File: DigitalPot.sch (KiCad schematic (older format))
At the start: 4 parts, among them IC24 AD5160BRJZ5-R2

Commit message: Checkpoint before trying 4 layer
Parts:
- IC24: footprint SOT65P280X145-8N -> Package_TO_SOT_SMD:SOT-23-8
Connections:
- no-connect marks 1 -> 2
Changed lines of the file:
@@
 $Descr A4 11693 8268
 encoding utf-8
-Sheet 40 50
+Sheet 23 37
 Title ""
 Date ""
@@
 AR Path="/60F3839B/60F38D7F" Ref="IC24"  Part="1"
 AR Path="/60F3F96F/60F38D7F" Ref="IC25"  Part="1"
-F 0 "IC25" H 5650 3915 50  0000 C CNN
+F 0 "IC24" H 5650 3915 50  0000 C CNN
 F 1 "AD5160BRJZ5-R2" H 5650 3824 50  0000 C CNN
-F 2 "SOT65P280X145-8N" H 6000 3750 50  0001 L CNN
+F 2 "Package_TO_SOT_SMD:SOT-23-8" H 6000 3750 50  0001 L CNN
 F 3 "http://www.analog.com/media/en/technical-documentation/data-sheets/AD5160.pdf" H 6000 3650 50  0001 L CNN
 F 4 "Dig Potentiometer 256 Pos 5KOhm Single" H 6000 3550 50  0001 L CNN "Description"
@@
 AR Path="/60F3839B/60F39459" Ref="C64"  Part="1"
 AR Path="/60F3F96F/60F39459" Ref="C68"  Part="1"
-F 0 "C68" H 4415 4046 50  0000 L CNN
+F 0 "C64" H 4415 4046 50  0000 L CNN
 F 1 "0.1uF" H 4415 3955 50  0000 L CNN
 F 2 "Capacitor_SMD:C_0805_2012Metric" H 4300 4000 50  0001 C CNN
@@
 AR Path="/60F3839B/60F3953A" Ref="C63"  Part="1"
 AR Path="/60F3F96F/60F3953A" Ref="C67"  Part="1"
-F 0 "C67" H 3915 4046 50  0000 L CNN
+F 0 "C63" H 3915 4046 50  0000 L CNN
 F 1 "10uF" H 3915 3955 50  0000 L CNN
 F 2 "Capacitor_SMD:C_0805_2012Metric" H 3800 4000 50  0001 C CNN
@@
 AR Path="/60F3839B/60F39721" Ref="C65"  Part="1"
 AR Path="/60F3F96F/60F39721" Ref="C69"  Part="1"
-F 0 "C69" H 7465 3596 50  0000 L CNN
+F 0 "C65" H 7465 3596 50  0000 L CNN
 F 1 "0.1uF" H 7465 3505 50  0000 L CNN
 F 2 "Capacitor_SMD:C_0805_2012Metric" H 7350 3550 50  0001 C CNN
@@
 Text HLabel 7550 4000 0    50   Input ~ 0
 GND
+NoConn ~ 4950 2450
 $EndSCHEMATC

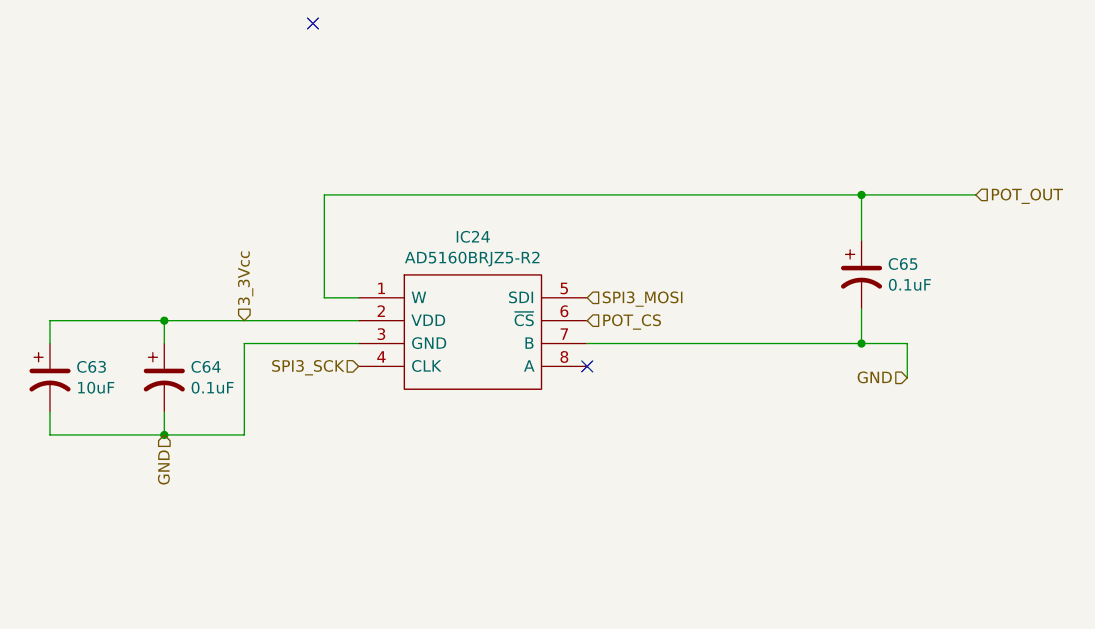
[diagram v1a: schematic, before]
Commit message: 4 layer board that passes checks
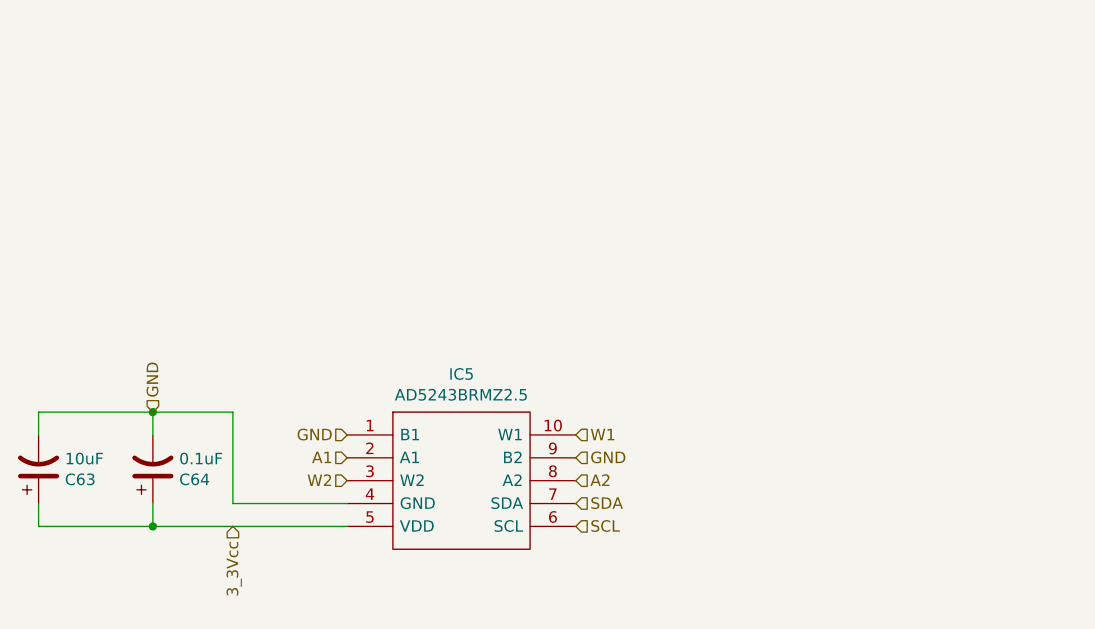
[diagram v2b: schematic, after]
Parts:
- removed C65: 0.1uF, Capacitor_SMD:C_0805_2012Metric, symbol Device:CP1
- removed IC24: AD5160BRJZ5-R2, Package_TO_SOT_SMD:SOT-23-8, symbol SamacSys_Parts:AD5160BRJZ5-R2
- added IC5: AD5243BRMZ2.5, SOP50P490X110-10N, symbol SamacSys_Parts:AD5243BRMZ2.5
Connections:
- net 3_3Vcc: now also IC5.5 (VDD)
- net GND: now also IC5.1 (B1), IC5.4 (GND), IC5.9 (B2)
- new net A1: IC5.2 (A1)
- new net A2: IC5.8 (A2)
- new net SCL: IC5.6 (SCL)
- new net SDA: IC5.7 (SDA)
- new net W1: IC5.10 (W1)
- new net W2: IC5.3 (W2)
- no-connect marks 2 -> 0
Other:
- moved on the sheet: C63, C64
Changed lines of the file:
@@
 $Descr A4 11693 8268
 encoding utf-8
-Sheet 23 37
+Sheet 23 36
 Title ""
 Date ""
@@
 $EndDescr
 $Comp
-L SamacSys_Parts:AD5160BRJZ5-R2 IC24
-U 1 1 60F38D7F
-P 5150 3650
-AR Path="/60F3839B/60F38D7F" Ref="IC24"  Part="1"
-AR Path="/60F3F96F/60F38D7F" Ref="IC25"  Part="1"
-F 0 "IC24" H 5650 3915 50  0000 C CNN
-F 1 "AD5160BRJZ5-R2" H 5650 3824 50  0000 C CNN
-F 2 "Package_TO_SOT_SMD:SOT-23-8" H 6000 3750 50  0001 L CNN
-F 3 "http://www.analog.com/media/en/technical-documentation/data-sheets/AD5160.pdf" H 6000 3650 50  0001 L CNN
-F 4 "Dig Potentiometer 256 Pos 5KOhm Single" H 6000 3550 50  0001 L CNN "Description"
-F 5 "1.45" H 6000 3450 50  0001 L CNN "Height"
-F 6 "584-AD5160BRJZ5-R2" H 6000 3350 50  0001 L CNN "Mouser Part Number"
-F 7 "https://www.mouser.co.uk/ProductDetail/Analog-Devices/AD5160BRJZ5-R2?qs=NmRFExCfTkG4GI7t5vj5JA%3D%3D" H 6000 3250 50  0001 L CNN "Mouser Price/Stock"
-F 8 "Analog Devices" H 6000 3150 50  0001 L CNN "Manufacturer_Name"
-F 9 "AD5160BRJZ5-R2" H 6000 3050 50  0001 L CNN "Manufacturer_Part_Number"
-	1    5150 3650
-	1    0    0    -1
-$EndComp
-$Comp
 L Device:CP1 C64
 U 1 1 60F39459
-P 4300 4000
+P 4250 4400
 AR Path="/60F3839B/60F39459" Ref="C64"  Part="1"
 AR Path="/60F3F96F/60F39459" Ref="C68"  Part="1"
-F 0 "C64" H 4415 4046 50  0000 L CNN
-F 1 "0.1uF" H 4415 3955 50  0000 L CNN
-F 2 "Capacitor_SMD:C_0805_2012Metric" H 4300 4000 50  0001 C CNN
-F 3 "~" H 4300 4000 50  0001 C CNN
-	1    4300 4000
-	1    0    0    -1
+F 0 "C64" H 4365 4446 50  0000 L CNN
+F 1 "0.1uF" H 4365 4355 50  0000 L CNN
+F 2 "Capacitor_SMD:C_0805_2012Metric" H 4250 4400 50  0001 C CNN
+F 3 "~" H 4250 4400 50  0001 C CNN
+	1    4250 4400
+	1    0    0    1
 $EndComp
 $Comp
 L Device:CP1 C63
 U 1 1 60F3953A
-P 3800 4000
+P 3750 4400
 AR Path="/60F3839B/60F3953A" Ref="C63"  Part="1"
 AR Path="/60F3F96F/60F3953A" Ref="C67"  Part="1"
-F 0 "C63" H 3915 4046 50  0000 L CNN
-F 1 "10uF" H 3915 3955 50  0000 L CNN
-F 2 "Capacitor_SMD:C_0805_2012Metric" H 3800 4000 50  0001 C CNN
-F 3 "~" H 3800 4000 50  0001 C CNN
-	1    3800 4000
+F 0 "C63" H 3865 4446 50  0000 L CNN
+F 1 "10uF" H 3865 4355 50  0000 L CNN
+F 2 "Capacitor_SMD:C_0805_2012Metric" H 3750 4400 50  0001 C CNN
+F 3 "~" H 3750 4400 50  0001 C CNN
+	1    3750 4400
+	1    0    0    1
+$EndComp
+Wire Wire Line
+	3750 4650 3750 4550
+Wire Wire Line
+	4250 4650 4250 4550
+Connection ~ 4250 4650
+Wire Wire Line
+	4250 4650 3750 4650
+Wire Wire Line
+	3750 4250 3750 4150
+Wire Wire Line
+	3750 4150 4250 4150
+Wire Wire Line
+	4600 4150 4600 4550
+Wire Wire Line
+	4600 4550 5100 4550
+Wire Wire Line
+	4250 4250 4250 4150
+Connection ~ 4250 4150
+Wire Wire Line
+	4250 4150 4600 4150
+Wire Wire Line
+	4250 4650 5100 4650
+Text HLabel 4600 4650 3    50   Input ~ 0
+3_3Vcc
+Text HLabel 4250 4150 1    50   Input ~ 0
+GND
+Text HLabel 6100 4650 2    50   Input ~ 0
+SCL
+Text HLabel 6100 4550 2    50   Input ~ 0
+SDA
+$Comp
+L SamacSys_Parts:AD5243BRMZ2.5 IC5
+U 1 1 6286902C
+P 5100 4250
+AR Path="/60F3839B/6286902C" Ref="IC5"  Part="1"
+AR Path="/60F3F96F/6286902C" Ref="IC?"  Part="1"
+F 0 "IC5" H 5600 4515 50  0000 C CNN
+F 1 "AD5243BRMZ2.5" H 5600 4424 50  0000 C CNN
+F 2 "SOP50P490X110-10N" H 5950 4350 50  0001 L CNN
+F 3 "https://datasheet.datasheetarchive.com/originals/distributors/Datasheets-4/DSA-69649.pdf" H 5950 4250 50  0001 L CNN
+F 4 "AD5243BRMZ2.5, Digital Potentiometer 2.5k 256-Position 2-channel Serial-2 Wire, Serial-I2C 10-Pin MSOP" H 5950 4150 50  0001 L CNN "Description"
+F 5 "1.1" H 5950 4050 50  0001 L CNN "Height"
+F 6 "584-AD5243BRMZ2.5" H 5950 3950 50  0001 L CNN "Mouser Part Number"
+F 7 "https://www.mouser.co.uk/ProductDetail/Analog-Devices/AD5243BRMZ25?qs=NmRFExCfTkF%2FoBz%2FYeO%252Bww%3D%3D" H 5950 3850 50  0001 L CNN "Mouser Price/Stock"
+F 8 "Analog Devices" H 5950 3750 50  0001 L CNN "Manufacturer_Name"
+F 9 "AD5243BRMZ2.5" H 5950 3650 50  0001 L CNN "Manufacturer_Part_Number"
+	1    5100 4250
 	1    0    0    -1
 $EndComp
-$Comp
-L Device:CP1 C65
-U 1 1 60F39721
-P 7350 3550
-AR Path="/60F3839B/60F39721" Ref="C65"  Part="1"
-AR Path="/60F3F96F/60F39721" Ref="C69"  Part="1"
-F 0 "C65" H 7465 3596 50  0000 L CNN
-F 1 "0.1uF" H 7465 3505 50  0000 L CNN
-F 2 "Capacitor_SMD:C_0805_2012Metric" H 7350 3550 50  0001 C CNN
-F 3 "~" H 7350 3550 50  0001 C CNN
-	1    7350 3550
-	1    0    0    -1
-$EndComp
-NoConn ~ 6150 3950
-Wire Wire Line
-	7550 3850 7550 4000
-Wire Wire Line
-	5150 3650 5000 3650
-Wire Wire Line
-	5000 3650 5000 3200
-Wire Wire Line
-	5000 3200 7350 3200
-Wire Wire Line
-	6150 3850 7350 3850
-Wire Wire Line
-	7350 3700 7350 3850
-Connection ~ 7350 3850
-Wire Wire Line
-	7350 3850 7550 3850
-Wire Wire Line
-	7350 3200 7350 3400
-Connection ~ 7350 3200
-Wire Wire Line
-	7350 3200 7850 3200
-Text HLabel 7850 3200 2    50   Input ~ 0
-POT_OUT
-Text HLabel 6150 3750 2    50   Input ~ 0
-POT_CS
-Text HLabel 6150 3650 2    50   Input ~ 0
-SPI3_MOSI
-Text HLabel 5150 3950 0    50   Input ~ 0
-SPI3_SCK
-Wire Wire Line
-	3800 3750 3800 3850
-Wire Wire Line
-	4300 3750 4300 3850
-Connection ~ 4300 3750
-Wire Wire Line
-	4300 3750 3800 3750
-Wire Wire Line
-	3800 4150 3800 4250
-Wire Wire Line
-	3800 4250 4300 4250
-Wire Wire Line
-	4650 4250 4650 3850
-Wire Wire Line
-	4650 3850 5150 3850
-Wire Wire Line
-	4300 4150 4300 4250
-Connection ~ 4300 4250
-Wire Wire Line
-	4300 4250 4650 4250
-Wire Wire Line
-	4300 3750 5150 3750
-Text HLabel 4650 3750 1    50   Input ~ 0
-3_3Vcc
-Text HLabel 4300 4250 3    50   Input ~ 0
+Text HLabel 6100 4350 2    50   Input ~ 0
 GND
-Text HLabel 7550 4000 0    50   Input ~ 0
+Text HLabel 5100 4250 0    50   Input ~ 0
 GND
-NoConn ~ 4950 2450
+Text HLabel 5100 4350 0    50   Input ~ 0
+A1
+Text HLabel 5100 4450 0    50   Input ~ 0
+W2
+Text HLabel 6100 4250 2    50   Input ~ 0
+W1
+Text HLabel 6100 4450 2    50   Input ~ 0
+A2
 $EndSCHEMATC

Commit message: Routed PCB
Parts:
- C63: JLCPCB_PN (none) -> C15850
- C64: JLCPCB_PN (none) -> C49678
- IC5: JLCPCB_PN (none) -> C143871
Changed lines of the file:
@@
 F 2 "Capacitor_SMD:C_0805_2012Metric" H 4250 4400 50  0001 C CNN
 F 3 "~" H 4250 4400 50  0001 C CNN
+F 4 "C49678" H 4250 4400 50  0001 C CNN "JLCPCB_PN"
 	1    4250 4400
 	1    0    0    1
@@
 F 2 "Capacitor_SMD:C_0805_2012Metric" H 3750 4400 50  0001 C CNN
 F 3 "~" H 3750 4400 50  0001 C CNN
+F 4 "C15850" H 3750 4400 50  0001 C CNN "JLCPCB_PN"
 	1    3750 4400
 	1    0    0    1
@@
 F 8 "Analog Devices" H 5950 3750 50  0001 L CNN "Manufacturer_Name"
 F 9 "AD5243BRMZ2.5" H 5950 3650 50  0001 L CNN "Manufacturer_Part_Number"
+F 10 "C143871" H 5100 4250 50  0001 C CNN "JLCPCB_PN"
 	1    5100 4250
 	1    0    0    -1

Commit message: Checkpoint 2022-01-19
Design with bluepill to run the heater since we lose some of the SPI
pins to the USB port on the STM32-H107.
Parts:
- IC5: footprint SOP50P490X110-10N -> SamacSys_Parts:SOP50P490X110-10N
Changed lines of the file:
@@
 $Descr A4 11693 8268
 encoding utf-8
-Sheet 23 36
+Sheet 23 37
 Title ""
 Date ""
@@
 F 0 "IC5" H 5600 4515 50  0000 C CNN
 F 1 "AD5243BRMZ2.5" H 5600 4424 50  0000 C CNN
-F 2 "SOP50P490X110-10N" H 5950 4350 50  0001 L CNN
+F 2 "SamacSys_Parts:SOP50P490X110-10N" H 5950 4350 50  0001 L CNN
 F 3 "https://datasheet.datasheetarchive.com/originals/distributors/Datasheets-4/DSA-69649.pdf" H 5950 4250 50  0001 L CNN
 F 4 "AD5243BRMZ2.5, Digital Potentiometer 2.5k 256-Position 2-channel Serial-2 Wire, Serial-I2C 10-Pin MSOP" H 5950 4150 50  0001 L CNN "Description"
